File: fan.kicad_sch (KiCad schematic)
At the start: 4 parts, among them J5 691137710002, U8 BSR802NL6327HTSA1

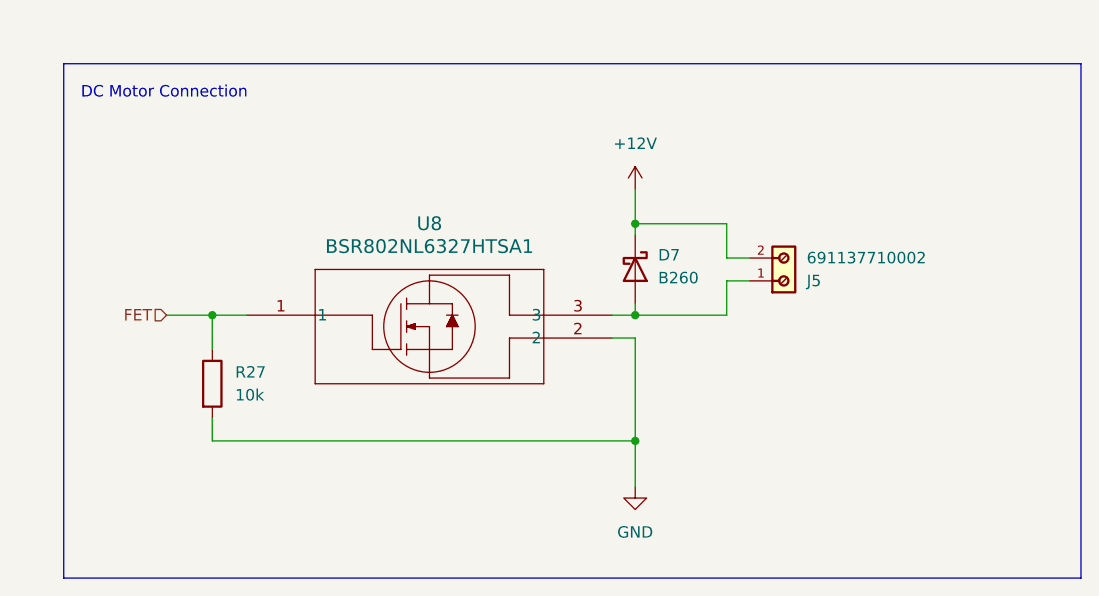
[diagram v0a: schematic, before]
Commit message: passed drc (somehow)
board routing is def cooked
verify:
- boost layout
- usb terminal layout
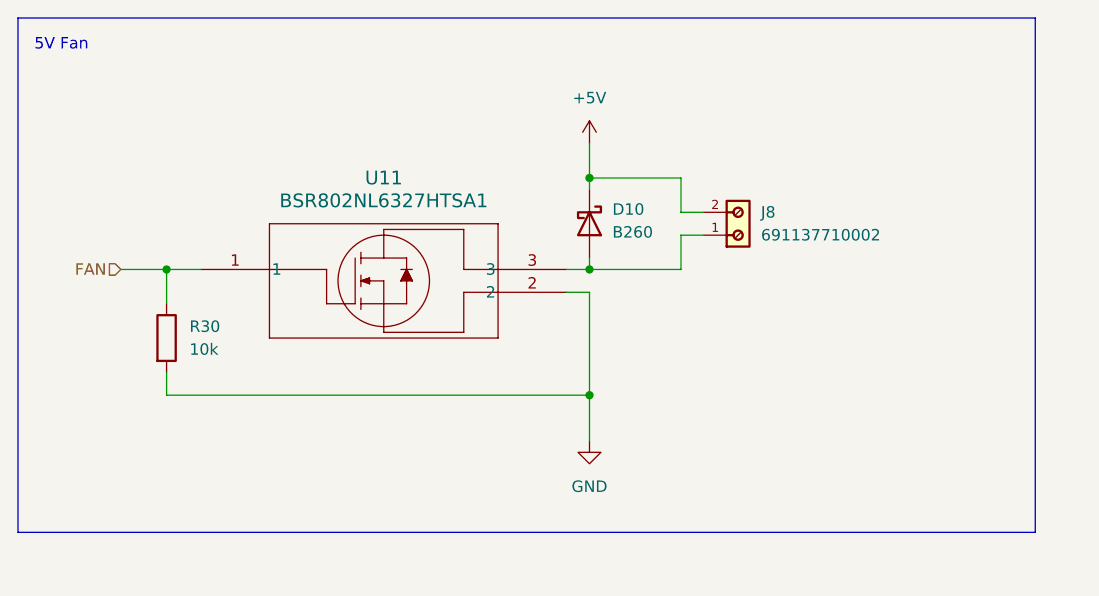
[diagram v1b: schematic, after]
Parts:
- removed D7: B260, Diode_SMD:D_SMB, symbol Diode:B260
- removed J5: 691137710002, footprints:691137710002, symbol 691137710002:691137710002
- removed R27: 10k, Resistor_SMD:R_0603_1608Metric, symbol Device:R
- removed U8: BSR802NL6327HTSA1, footprints:mosfet, symbol mosfet:BSR802NL6327HTSA1
- added D10: B260, Diode_SMD:D_SMB, symbol Diode:B260
- added J8: 691137710002, footprints:691137710002, symbol 691137710002:691137710002
- added R30: 10k, Resistor_SMD:R_0603_1608Metric, symbol Device:R
- added U11: BSR802NL6327HTSA1, footprints:mosfet, symbol mosfet:BSR802NL6327HTSA1
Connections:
- net GND: now also R30.2, U11.2
- new net: D10.2 (A), J8.1, U11.3
- new net +5V: D10.1 (K), J8.2
- new net FAN: R30.1, U11.1
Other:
- note added: "5V Fan"
- note removed: "DC Motor Connection"
